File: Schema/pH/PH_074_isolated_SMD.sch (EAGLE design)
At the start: 31 parts, among them IC1 TL074D, IC2 TLC271D

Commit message: update pH schema and board
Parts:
- added R13: 1k, rcl:R-EU_R1206W
- R8: device rcl:R-EU_R0805W -> rcl:R-EU_R1206W
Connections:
- new net NIC: C7.1, IC2.OUT, R11.1, R13.2
- net GND: now also LED1.A
- net N$1: now also TRIM2.2; no longer TRIM2.1
- net N$12: now also TRIM1.2; no longer TRIM1.1
- net OUTPUT: now also R13.1; no longer C7.1, IC2.OUT, R11.1
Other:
- moved on the sheet: TRIM1, TRIM2
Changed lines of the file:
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@@
 <part name="GND6" library="supply1" deviceset="GND" device=""/>
 <part name="GND8" library="supply1" deviceset="GND" device=""/>
-<part name="R8" library="rcl" deviceset="R-EU_" device="R0805W" value="3k3"/>
+<part name="R8" library="rcl" deviceset="R-EU_" device="R1206W" value="3k3"/>
 <part name="D1" library="Sensuino" deviceset="1N4148" device=""/>
 <part name="LED1" library="candrian" deviceset="LED" device="3MM"/>
@@
 <part name="GND9" library="supply1" deviceset="GND" device=""/>
 <part name="U$1" library="Sensuino" deviceset="ZENER" device=""/>
+<part name="R13" library="rcl" deviceset="R-EU_" device="R1206W" value="1k"/>
 </parts>
 <sheets>
@@
 <instance part="R1" gate="G$1" x="5.08" y="25.4"/>
 <instance part="R2" gate="G$1" x="17.78" y="10.16"/>
-<instance part="TRIM1" gate="1" x="33.02" y="10.16" rot="R270"/>
-<instance part="TRIM2" gate="1" x="48.26" y="63.5" rot="R90"/>
+<instance part="TRIM1" gate="1" x="30.48" y="10.16" rot="MR90"/>
+<instance part="TRIM2" gate="1" x="48.26" y="63.5" rot="MR270"/>
 <instance part="R3" gate="G$1" x="40.64" y="27.94"/>
 <instance part="R5" gate="G$1" x="20.32" y="48.26" rot="R90"/>
@@
 <instance part="C8" gate="G$1" x="154.94" y="7.62" rot="R270"/>
 <instance part="GND9" gate="1" x="2.54" y="50.8"/>
-<instance part="U$1" gate="G$1" x="180.34" y="7.62" rot="R90"/>
+<instance part="U$1" gate="G$1" x="193.04" y="7.62" rot="R90"/>
+<instance part="R13" gate="G$1" x="180.34" y="17.78" rot="R180"/>
 </instances>
 <busses>
@@
 <wire x1="15.24" y1="17.78" x2="15.24" y2="20.32" width="0.1524" layer="91"/>
 <pinref part="GND7" gate="1" pin="GND"/>
+</segment>
+<segment>
+<pinref part="GND9" gate="1" pin="GND"/>
+<pinref part="LED1" gate="G$1" pin="A"/>
+<wire x1="2.54" y1="53.34" x2="5.08" y2="53.34" width="0.1524" layer="91"/>
 </segment>
 </net>
@@
 <net name="N$12" class="0">
 <segment>
-<wire x1="30.48" y1="27.94" x2="33.02" y2="27.94" width="0.1524" layer="91"/>
 <pinref part="R3" gate="G$1" pin="1"/>
 <pinref part="IC1" gate="A" pin="OUT"/>
-<pinref part="TRIM1" gate="1" pin="1"/>
-<wire x1="33.02" y1="27.94" x2="35.56" y2="27.94" width="0.1524" layer="91"/>
-<wire x1="33.02" y1="15.24" x2="33.02" y2="27.94" width="0.1524" layer="91"/>
-<junction x="33.02" y="27.94"/>
+<wire x1="30.48" y1="27.94" x2="35.56" y2="27.94" width="0.1524" layer="91"/>
+<pinref part="TRIM1" gate="1" pin="2"/>
+<wire x1="30.48" y1="15.24" x2="30.48" y2="27.94" width="0.1524" layer="91"/>
 </segment>
 </net>
@@
 <wire x1="48.26" y1="53.34" x2="45.72" y2="53.34" width="0.1524" layer="91"/>
 <pinref part="R8" gate="G$1" pin="2"/>
-<pinref part="TRIM2" gate="1" pin="1"/>
+<pinref part="TRIM2" gate="1" pin="2"/>
 <wire x1="48.26" y1="53.34" x2="48.26" y2="58.42" width="0.1524" layer="91"/>
-<junction x="48.26" y="53.34"/>
 </segment>
 </net>
@@
 </segment>
 </net>
-<net name="OUTPUT" class="0">
+<net name="NIC" class="0">
 <segment>
 <wire x1="172.72" y1="38.1" x2="172.72" y2="33.02" width="0.1524" layer="91"/>
@@
 <wire x1="172.72" y1="33.02" x2="172.72" y2="17.78" width="0.1524" layer="91"/>
 <wire x1="172.72" y1="17.78" x2="167.64" y2="17.78" width="0.1524" layer="91"/>
-<wire x1="172.72" y1="17.78" x2="177.8" y2="17.78" width="0.1524" layer="91"/>
 <pinref part="C7" gate="G$1" pin="1"/>
-<wire x1="177.8" y1="17.78" x2="180.34" y2="17.78" width="0.1524" layer="91"/>
 <wire x1="157.48" y1="38.1" x2="172.72" y2="38.1" width="0.1524" layer="91"/>
 <pinref part="R11" gate="G$1" pin="1"/>
 <wire x1="170.18" y1="33.02" x2="172.72" y2="33.02" width="0.1524" layer="91"/>
 <junction x="172.72" y="33.02"/>
-<label x="180.34" y="17.78" size="1.778" layer="95"/>
-<pinref part="U$1" gate="G$1" pin="CATHODE"/>
-<junction x="177.8" y="17.78"/>
-</segment>
-<segment>
-<label x="38.1" y="66.04" size="1.778" layer="95"/>
-<wire x1="38.1" y1="66.04" x2="38.1" y2="71.12" width="0.1524" layer="91"/>
-<pinref part="RJ" gate="G$1" pin="4"/>
-<wire x1="38.1" y1="71.12" x2="43.18" y2="71.12" width="0.1524" layer="91"/>
+<pinref part="R13" gate="G$1" pin="2"/>
+<wire x1="172.72" y1="17.78" x2="175.26" y2="17.78" width="0.1524" layer="91"/>
 </segment>
 </net>
@@
 <segment>
 <pinref part="U$1" gate="G$1" pin="ANODE"/>
-<wire x1="177.8" y1="-12.7" x2="177.8" y2="-17.78" width="0.1524" layer="91"/>
+<wire x1="190.5" y1="-12.7" x2="190.5" y2="-20.32" width="0.1524" layer="91"/>
+<label x="190.5" y="-20.32" size="1.778" layer="95"/>
 </segment>
 </net>
@@
 <wire x1="63.5" y1="50.8" x2="71.12" y2="50.8" width="0.1524" layer="91"/>
 <wire x1="71.12" y1="63.5" x2="71.12" y2="50.8" width="0.1524" layer="91"/>
+<pinref part="R12" gate="G$1" pin="2"/>
+<wire x1="71.12" y1="48.26" x2="71.12" y2="50.8" width="0.1524" layer="91"/>
 <pinref part="TRIM2" gate="1" pin="3"/>
 <wire x1="53.34" y1="63.5" x2="71.12" y2="63.5" width="0.1524" layer="91"/>
-<pinref part="R12" gate="G$1" pin="2"/>
-<wire x1="71.12" y1="48.26" x2="71.12" y2="50.8" width="0.1524" layer="91"/>
 </segment>
 </net>
@@
 <wire x1="48.26" y1="33.02" x2="48.26" y2="38.1" width="0.1524" layer="91"/>
 <pinref part="R12" gate="G$1" pin="1"/>
-</segment>
-</net>
-<net name="N$5" class="0">
-<segment>
-<pinref part="R2" gate="G$1" pin="2"/>
-<pinref part="TRIM1" gate="1" pin="3"/>
-<wire x1="22.86" y1="10.16" x2="27.94" y2="10.16" width="0.1524" layer="91"/>
 </segment>
 </net>
@@
 </segment>
 </net>
+<net name="N$5" class="0">
+<segment>
+<pinref part="R2" gate="G$1" pin="2"/>
+<pinref part="TRIM1" gate="1" pin="3"/>
+<wire x1="22.86" y1="10.16" x2="25.4" y2="10.16" width="0.1524" layer="91"/>
+</segment>
+</net>
+<net name="OUTPUT" class="0">
+<segment>
+<pinref part="R13" gate="G$1" pin="1"/>
+<wire x1="185.42" y1="17.78" x2="190.5" y2="17.78" width="0.1524" layer="91"/>
+<pinref part="U$1" gate="G$1" pin="CATHODE"/>
+<wire x1="190.5" y1="17.78" x2="198.12" y2="17.78" width="0.1524" layer="91"/>
+<junction x="190.5" y="17.78"/>
+<label x="198.12" y="17.78" size="1.778" layer="95"/>
+</segment>
+<segment>
+<label x="38.1" y="66.04" size="1.778" layer="95"/>
+<wire x1="38.1" y1="66.04" x2="38.1" y2="71.12" width="0.1524" layer="91"/>
+<pinref part="RJ" gate="G$1" pin="4"/>
+<wire x1="38.1" y1="71.12" x2="43.18" y2="71.12" width="0.1524" layer="91"/>
+</segment>
+</net>

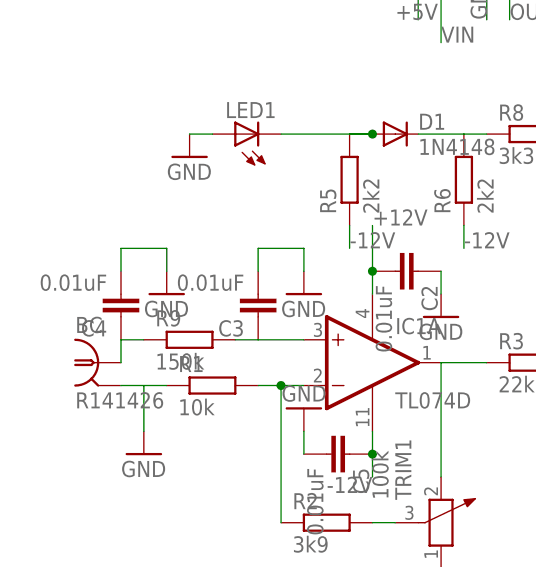
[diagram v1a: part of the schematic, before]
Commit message: C3 and C4 corrected values
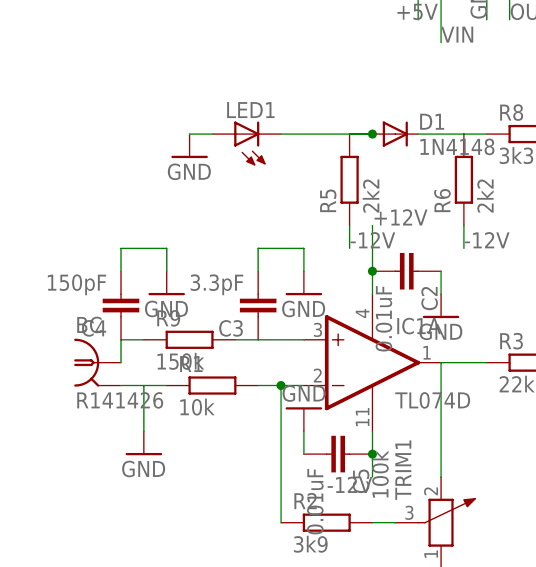
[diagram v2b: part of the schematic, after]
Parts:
- C3: value 0.01uF -> 3.3pF
- C4: value 0.01uF -> 150pF
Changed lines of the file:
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@@
 <?xml version="1.0" encoding="utf-8"?>
 <!DOCTYPE eagle SYSTEM "eagle.dtd">
-<eagle version="6.4">
+<eagle version="6.6.0">
 <drawing>
 <settings>
@@
 <part name="IC1" library="linear" deviceset="TL074" device="D"/>
 <part name="R9" library="rcl" deviceset="R-EU_" device="R0805W" value="150k"/>
-<part name="C3" library="rcl" deviceset="C-EU" device="C0805" value="0.01uF"/>
-<part name="C4" library="rcl" deviceset="C-EU" device="C0805" value="0.01uF"/>
+<part name="C3" library="rcl" deviceset="C-EU" device="C0805" value="3.3pF"/>
+<part name="C4" library="rcl" deviceset="C-EU" device="C0805" value="150pF"/>
 <part name="GND5" library="supply1" deviceset="GND" device=""/>
 <part name="GND6" library="supply1" deviceset="GND" device=""/>
